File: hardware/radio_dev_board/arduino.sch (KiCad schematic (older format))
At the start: 20 parts

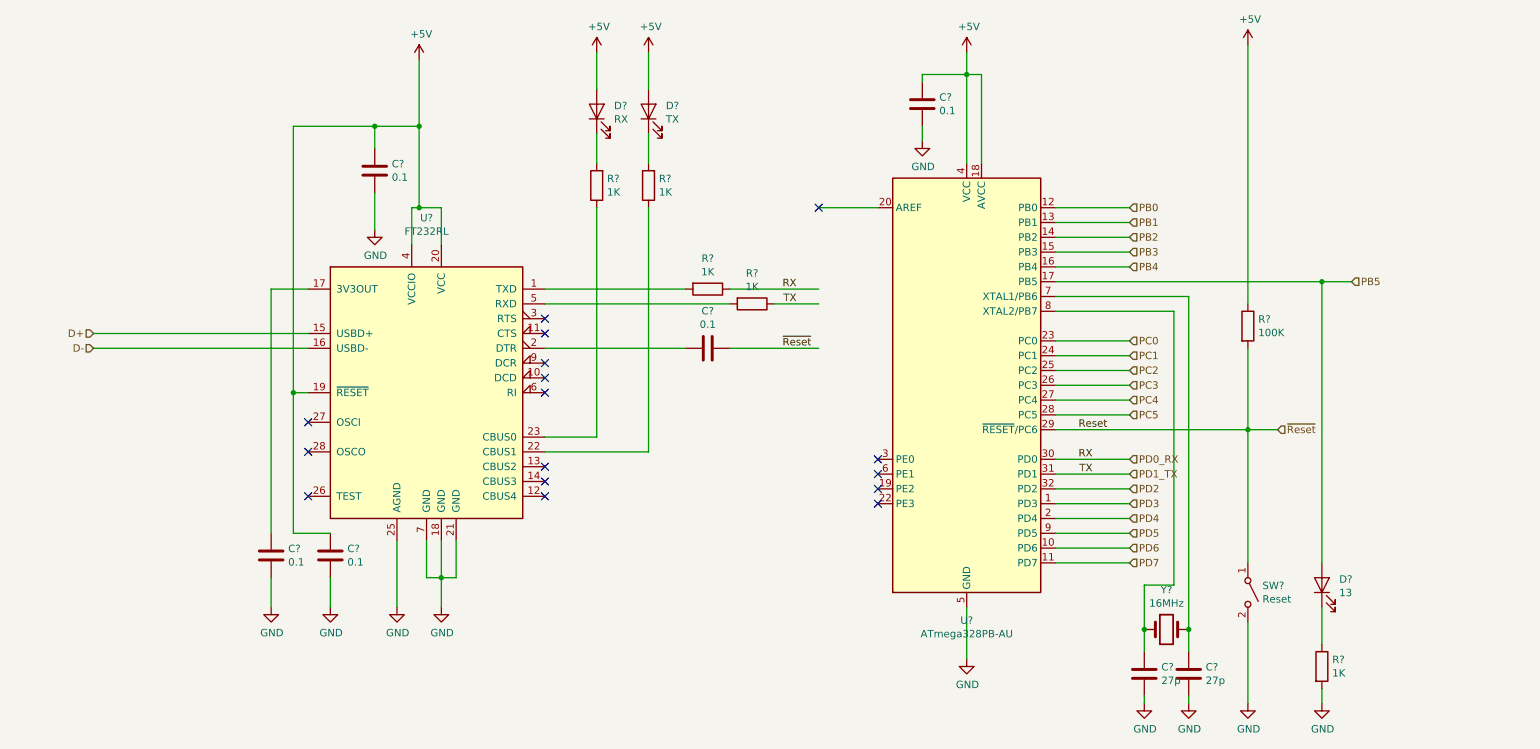
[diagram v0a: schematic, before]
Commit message: added radio USB serial channel. Update board layout
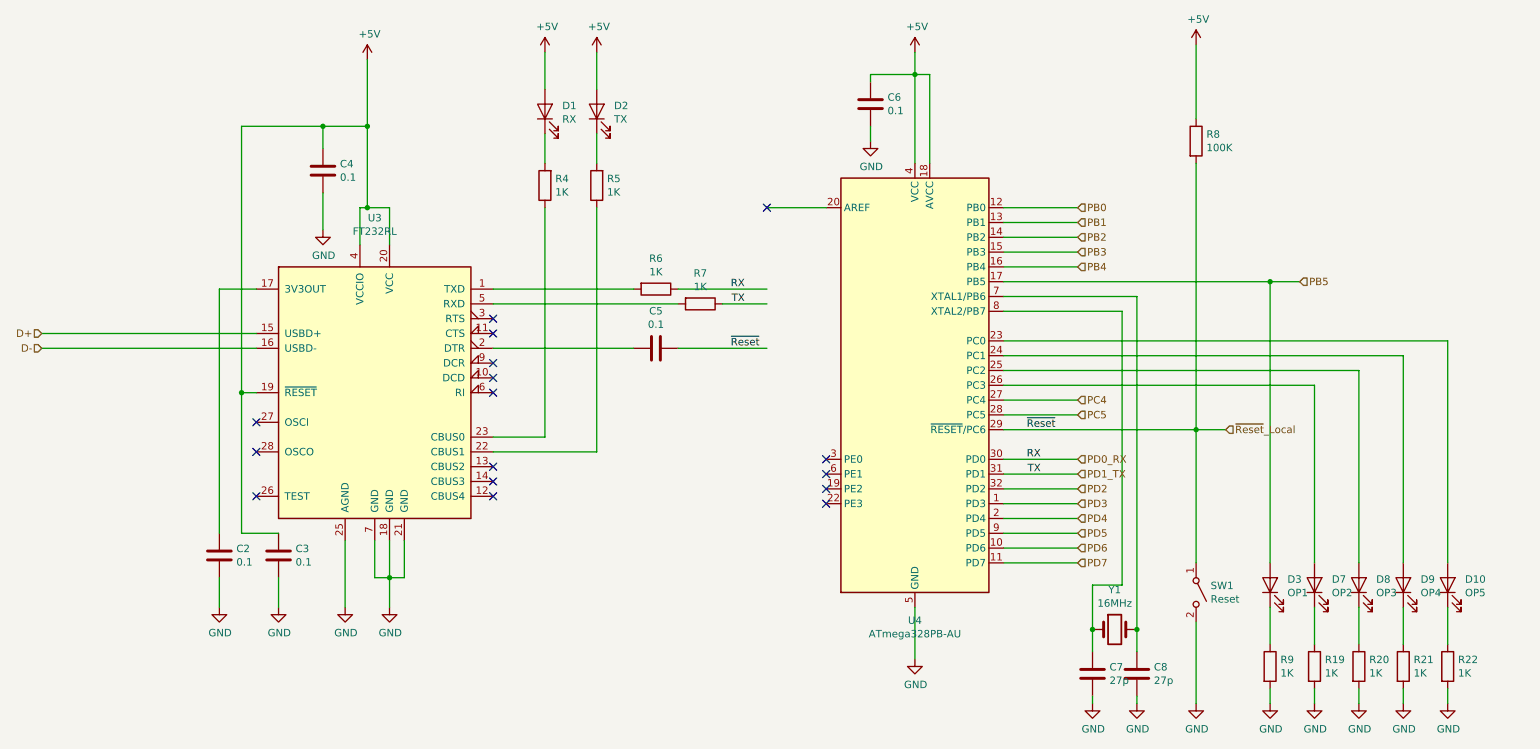
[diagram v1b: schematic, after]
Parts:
- added D10: OP5, LED_SMD:LED_0603_1608Metric_Pad1.05x0.95mm_HandSolder, symbol Device:LED
- added D7: OP2, LED_SMD:LED_0603_1608Metric_Pad1.05x0.95mm_HandSolder, symbol Device:LED
- added D8: OP3, LED_SMD:LED_0603_1608Metric_Pad1.05x0.95mm_HandSolder, symbol Device:LED
- added D9: OP4, LED_SMD:LED_0603_1608Metric_Pad1.05x0.95mm_HandSolder, symbol Device:LED
- added R19, R20, R21, R22: 1K, Resistor_SMD:R_0603_1608Metric_Pad1.05x0.95mm_HandSolder, symbol Device:R
- D3: renamed from D?; value 13 -> OP1
- Y1: renamed from Y?; footprint Crystal:Crystal_HC49-U_Vertical -> Crystal:Crystal_HC49-4H_Vertical
- gave numbers to parts that had none: 18
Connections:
- net labels added: ~Reset~_Local
- net labels removed: PC0, PC1, PC2, PC3, Reset
- wire segments 90 -> 102
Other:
- moved on the sheet: C2, C3, C4, C5, C6, C7, C8, D1, D2, D3, R4, R5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

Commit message: added program and misc buttons. Finish layout
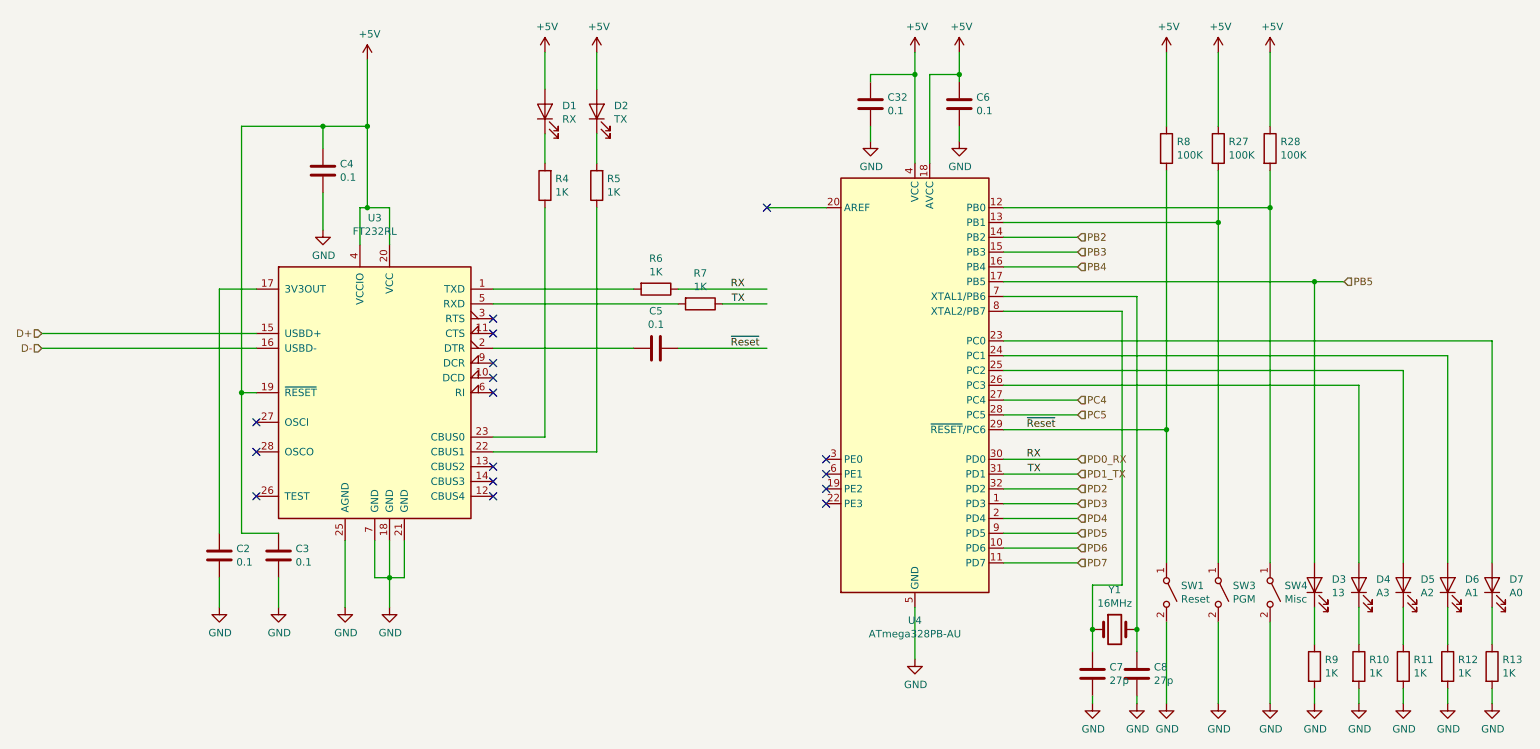
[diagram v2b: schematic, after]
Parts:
- added C32: 0.1, Capacitor_SMD:C_0603_1608Metric_Pad1.05x0.95mm_HandSolder, symbol Device:C
- added R27, R28: 100K, Resistor_SMD:R_0603_1608Metric_Pad1.05x0.95mm_HandSolder, symbol Device:R
- added SW3: PGM, Button_Switch_SMD:SW_SPST_PTS645, symbol Switch:SW_SPST
- added SW4: Misc, Button_Switch_SMD:SW_SPST_PTS645, symbol Switch:SW_SPST
- D3: value OP1 -> 13
- D4: renamed from D7; value OP2 -> A3
- D5: renamed from D8; value OP3 -> A2
- D6: renamed from D9; value OP4 -> A1
- D7: renamed from D10; value OP5 -> A0
- renumbered R19 to R10, R20 to R11, R21 to R12, R22 to R13
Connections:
- net +5V: now also C32.1, R27.1, R28.1
- net GND: now also C32.2, SW3.2 (B), SW4.2 (B)
- net PB0: no longer names the net of U4.12 (PB0)
- net PB0: now also R28.2, SW4.1 (A)
- net PB1: no longer names the net of U4.13 (PB1)
- net PB1: now also R27.2, SW3.1 (A)
- net ~Reset~_Local renamed ~Reset
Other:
- moved on the sheet: C6, D3, D4, D5, D6, D7, R10, R11, R12, R13, R8, R9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

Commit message: radio hub board started
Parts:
- U3: symbol Interface_USB:FT232RL -> radioDev-rescue:FT232RL-Interface_USB
- U4: symbol MCU_Microchip_ATmega:ATmega328PB-AU -> radioDev-rescue:ATmega328PB-AU-MCU_Microchip_ATmega
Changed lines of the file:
@@
 EESchema Schematic File Version 4
-LIBS:radioDev-cache
 EELAYER 30 0
 EELAYER END
@@
 $EndDescr
 $Comp
-L Interface_USB:FT232RL U3
+L radioDev-rescue:FT232RL-Interface_USB U3
 U 1 1 5D71F5F1
 P 3400 3700
@@
 NoConn ~ 2600 4400
 $Comp
-L MCU_Microchip_ATmega:ATmega328PB-AU U4
+L radioDev-rescue:ATmega328PB-AU-MCU_Microchip_ATmega U4
 U 1 1 5D8F30F9
 P 7050 3650
